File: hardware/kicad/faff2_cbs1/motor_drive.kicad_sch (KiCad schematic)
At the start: 89 parts, among them J1101 1x6 2.54mm, J1102 1x6 2.54mm, J1103 Micro-Fit 1x3, Q1101 BSZ099N06LS5, Q1102 BSZ099N06LS5, Q1103 BSZ099N06LS5, Q1104 BSZ099N06LS5, Q1105 BSZ099N06LS5, Q1106 BSZ099N06LS5, U1101 DRV8323S

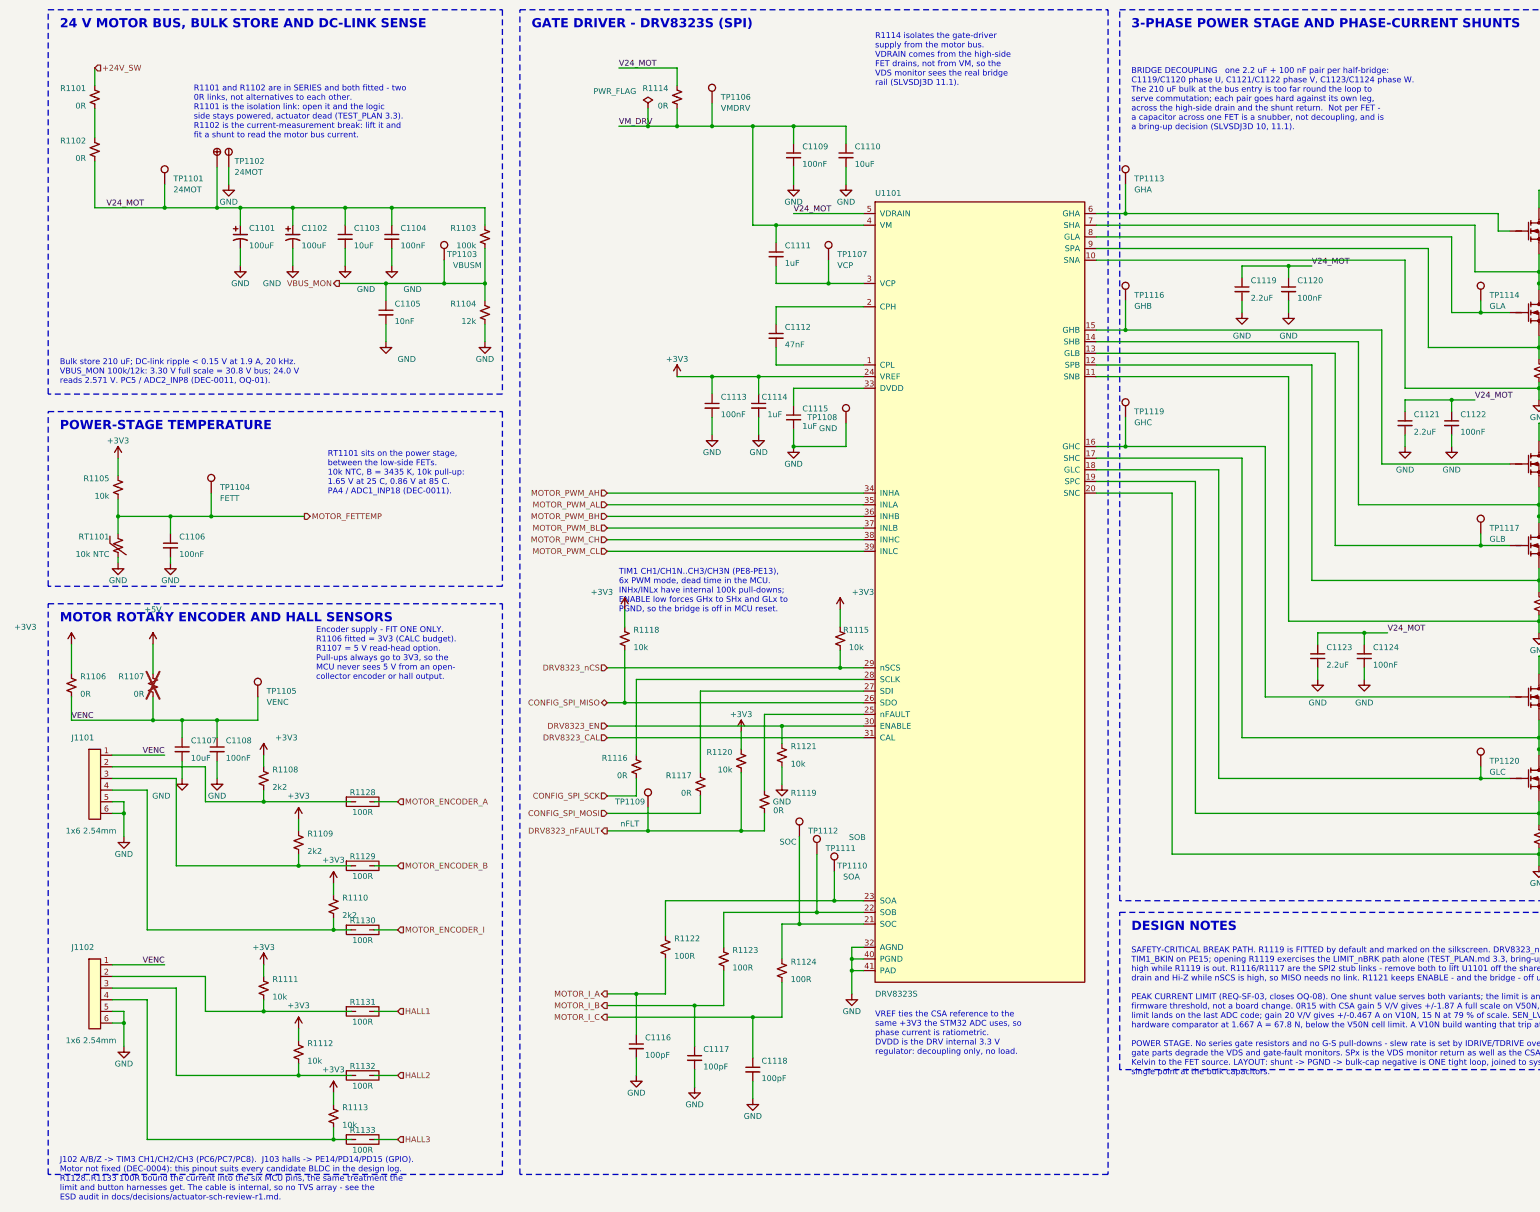
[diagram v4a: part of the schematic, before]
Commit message: review r2 item 8: one placement rule for every power symbol's net name
"Directly above it, centre justified, and close" - applied as no sideways
offset, centred, 3.81 mm away: above a rail arrow, below a ground. All 283
power symbols now carry it; 103 did not, most left-anchored rather than centred
and a few offset up to 7.6 mm sideways by round 1's auto-placer.

The ground mirror is an interpretation and is flagged as such: "above" a GND
symbol is where its wire arrives, and 137 instances plus every convention put
GND's name under the triangle. One line to change if the captain meant it
literally.

What makes this different from round 1 is that the label is now PINNED, so
everything else moves instead - the symbol along its own stub, a note to the
nearest clear spot, a block box outward (five rectangles grew where a name sat
on a border with clear space beyond), and two PWR_FLAGs placed by hand because
their 9.5 mm names do not fit the 10 mm rail runs they tap.

Thirteen of 283 still graze a wire, body or note on the two densest sheets and
are listed in the decisions file rather than hidden. Each needs the parts around
it respaced, which is more than a label sweep should do unasked - the TIM1 note
on motor_drive in particular has nowhere to go: no clear position exists for a
47.6 x 8.7 mm box anywhere in that block.

Also recorded: my own severity metric scored wire-through-text at zero for a
while, because a wire is a zero-thickness segment and box-intersection depth
against it is always 0. For those, severity is how far inside the box the line
sits. A render caught it; the number did not.

ERC 0 errors / 0 warnings at severity-all; 412 components, 259 nets, node sets
identical to before the batch. Review PDF regenerated once, here, for the whole
of round 2.

Co-Authored-By: Claude Opus 5 <noreply@anthropic.com>
Claude-Session: https://claude.ai/code/session_01PFWfwT8RZc8Zqn8vgZxV8j
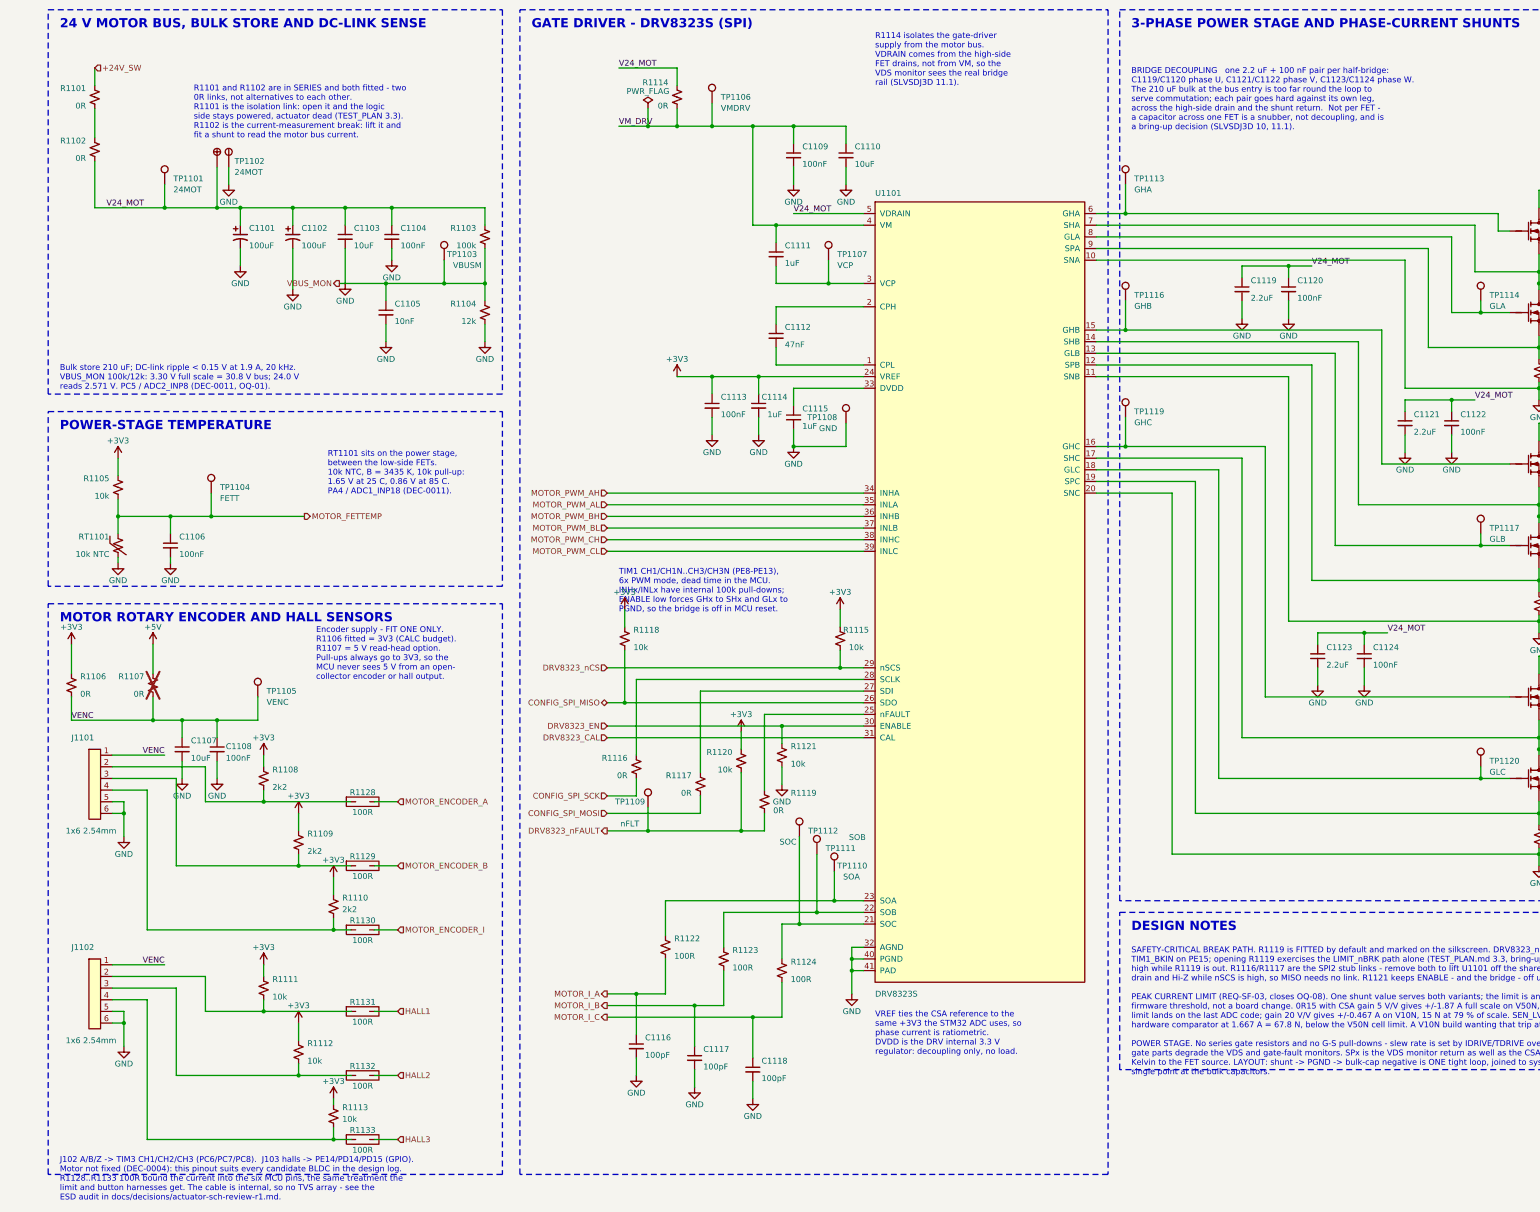
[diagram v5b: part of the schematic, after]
